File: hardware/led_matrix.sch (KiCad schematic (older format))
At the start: 16 parts

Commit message: Rev5 schematic changes and pcb cleanup
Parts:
- added R11, R26, R6: R, Resistor_SMD:R_0603_1608Metric, symbol Device:R
- added U10, U11, U9: SM16106, Package_SO:QSOP-24_3.9x8.7mm_P0.635mm, symbol rgbchip:SM16106
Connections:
- net L2 is gone; now on net VCC: D43.4 (A), D47.4 (A)
- net L3 is gone; now on net VCC: D36.4 (A), D40.4 (A)
- net L4 is gone; now on net VCC: D44.4 (A), D48.4 (A)
- net L5 is gone; now on net VCC: D37.4 (A), D41.4 (A)
- net L6 is gone; now on net VCC: D45.4 (A), D49.4 (A)
- net L7 is gone; now on net VCC: D38.4 (A), D42.4 (A)
- net L8 is gone; now on net VCC: D46.4 (A), D50.4 (A)
- net B1: now also U11.5 (OUT0); no longer D36.3 (BK), D37.3 (BK), D38.3 (BK), D43.3 (BK), D44.3 (BK), D45.3 (BK), D46.3 (BK)
- net B2: now also U11.6 (OUT1); no longer D40.3 (BK), D41.3 (BK), D42.3 (BK), D47.3 (BK), D48.3 (BK), D49.3 (BK), D50.3 (BK)
- net G1: now also U10.5 (OUT0); no longer D36.2 (GK), D37.2 (GK), D38.2 (GK), D43.2 (GK), D44.2 (GK), D45.2 (GK), D46.2 (GK)
- net G2: now also U10.6 (OUT1); no longer D40.2 (GK), D41.2 (GK), D42.2 (GK), D47.2 (GK), D48.2 (GK), D49.2 (GK), D50.2 (GK)
- net R1: now also U9.5 (OUT0); no longer D36.1 (RK), D37.1 (RK), D38.1 (RK), D43.1 (RK), D44.1 (RK), D45.1 (RK), D46.1 (RK)
- net R2: now also U9.6 (OUT1); no longer D40.1 (RK), D41.1 (RK), D42.1 (RK), D47.1 (RK), D48.1 (RK), D49.1 (RK), D50.1 (RK)
- net L1 renamed VCC
- net VCC: now also U10.24 (VDD), U11.24 (VDD), U9.24 (VDD)
- new net: U10.2 (SDI), U9.22 (SDO)
- new net: R6.1, U9.23 (R-EXT)
- new net: U10.22 (SDO), U11.2 (SDI)
- new net: R26.1, U11.23 (R-EXT)
- new net: R11.1, U10.23 (R-EXT)
- new net B10: D41.3 (BK), U11.14 (OUT9)
- new net B11: D45.3 (BK), U11.15 (OUT10)
- new net B12: D49.3 (BK), U11.16 (OUT11)
- new net B13: D38.3 (BK), U11.17 (OUT12)
- new net B14: D42.3 (BK), U11.18 (OUT13)
- new net B15: D46.3 (BK), U11.19 (OUT14)
- new net B16: D50.3 (BK), U11.20 (OUT15)
- new net B3: D43.3 (BK), U11.7 (OUT2)
- new net B4: D47.3 (BK), U11.8 (OUT3)
- new net B5: D36.3 (BK), U11.9 (OUT4)
- new net B6: D40.3 (BK), U11.10 (OUT5)
- new net B7: D44.3 (BK), U11.11 (OUT6)
- new net B8: D48.3 (BK), U11.12 (OUT7)
- new net B9: D37.3 (BK), U11.13 (OUT8)
- new net CLK: U10.3 (CLK), U11.3 (CLK), U9.3 (CLK)
- new net G10: D41.2 (GK), U10.14 (OUT9)
- new net G11: D45.2 (GK), U10.15 (OUT10)
- new net G12: D49.2 (GK), U10.16 (OUT11)
- new net G13: D38.2 (GK), U10.17 (OUT12)
- new net G14: D42.2 (GK), U10.18 (OUT13)
- new net G15: D46.2 (GK), U10.19 (OUT14)
- new net G16: D50.2 (GK), U10.20 (OUT15)
- new net G3: D43.2 (GK), U10.7 (OUT2)
- new net G4: D47.2 (GK), U10.8 (OUT3)
- new net G5: D36.2 (GK), U10.9 (OUT4)
- new net G6: D40.2 (GK), U10.10 (OUT5)
- new net G7: D44.2 (GK), U10.11 (OUT6)
- new net G8: D48.2 (GK), U10.12 (OUT7)
- new net G9: D37.2 (GK), U10.13 (OUT8)
- new net GND: R11.2, R26.2, R6.2, U10.1 (GND), U11.1 (GND), U9.1 (GND)
- new net LE: U10.4 (LE), U11.4 (LE), U9.4 (LE)
- new net OE: U10.21 (OE), U11.21 (OE), U9.21 (OE)
- new net R10: D41.1 (RK), U9.14 (OUT9)
- new net R11: D45.1 (RK), U9.15 (OUT10)
- new net R12: D49.1 (RK), U9.16 (OUT11)
- new net R13: D38.1 (RK), U9.17 (OUT12)
- new net R14: D42.1 (RK), U9.18 (OUT13)
- new net R15: D46.1 (RK), U9.19 (OUT14)
- new net R16: D50.1 (RK), U9.20 (OUT15)
- new net R3: D43.1 (RK), U9.7 (OUT2)
- new net R4: D47.1 (RK), U9.8 (OUT3)
- new net R5: D36.1 (RK), U9.9 (OUT4)
- new net R6: D40.1 (RK), U9.10 (OUT5)
- new net R7: D44.1 (RK), U9.11 (OUT6)
- new net R8: D48.1 (RK), U9.12 (OUT7)
- new net R9: D37.1 (RK), U9.13 (OUT8)
- new net SDI: U9.2 (SDI)
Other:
- moved on the sheet: D35, D36, D37, D38, D39, D40, D41, D42, D43, D44, D45, D46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

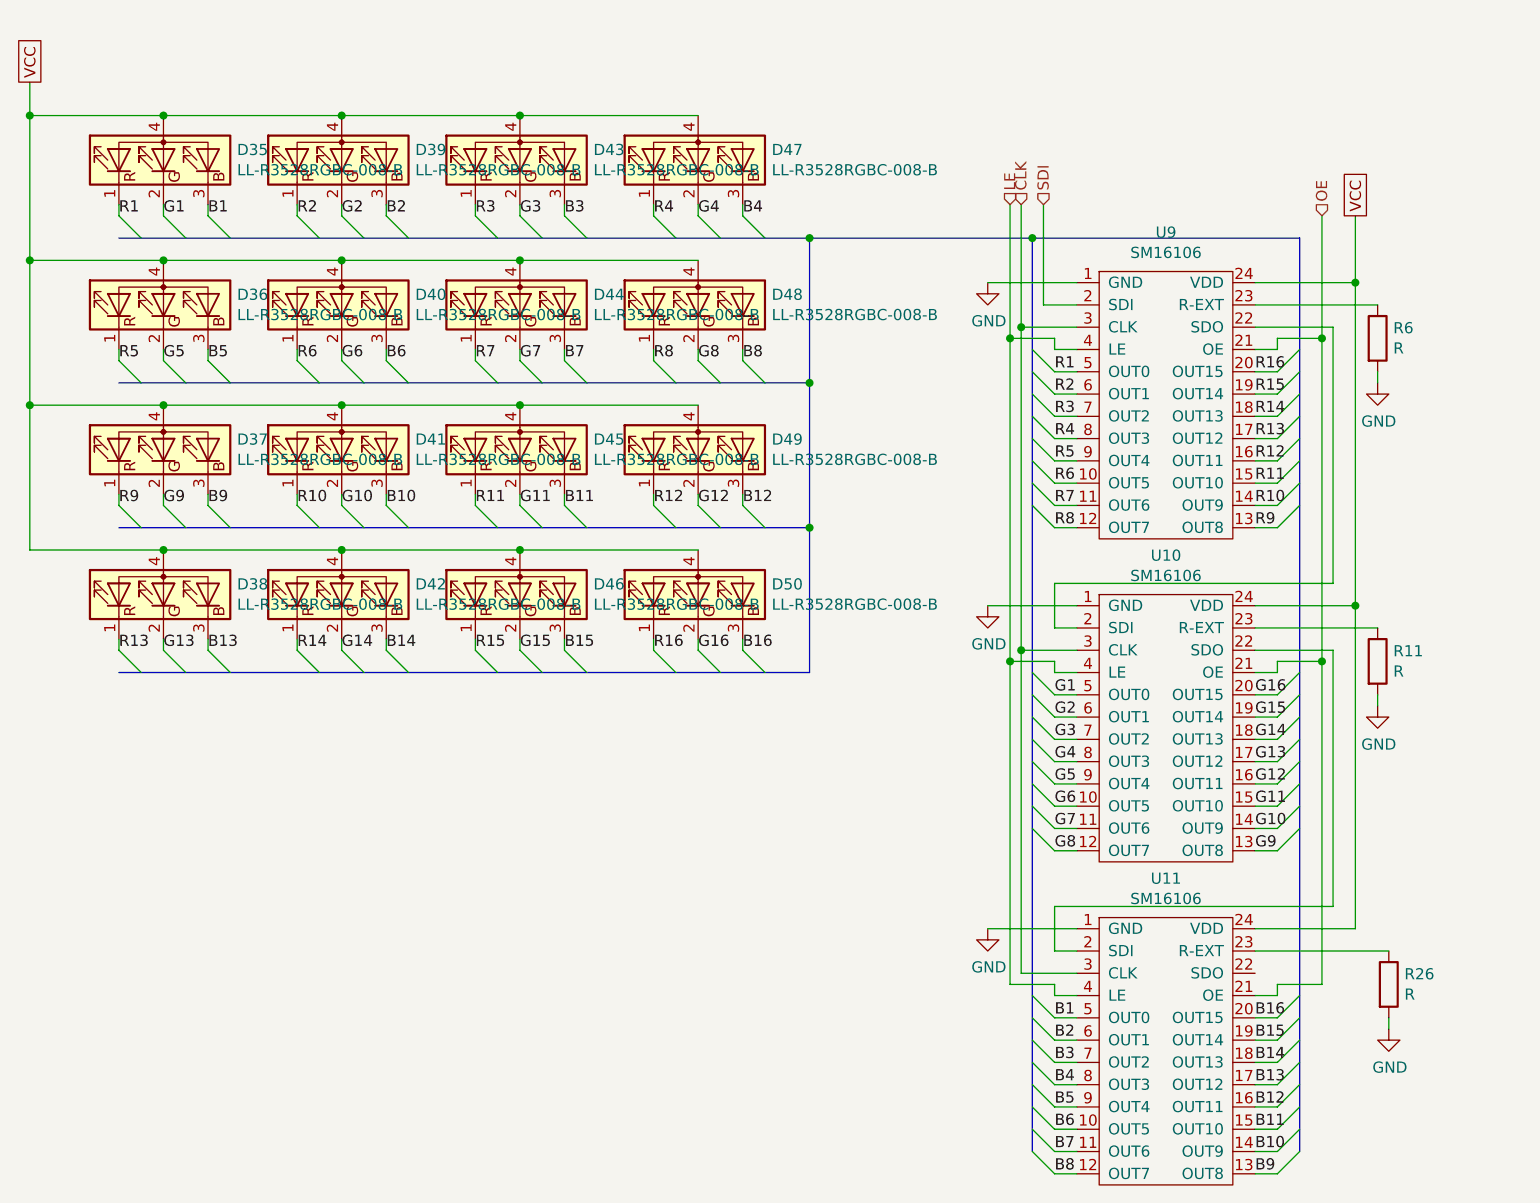
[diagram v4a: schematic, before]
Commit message: Major routing of the led matrix done
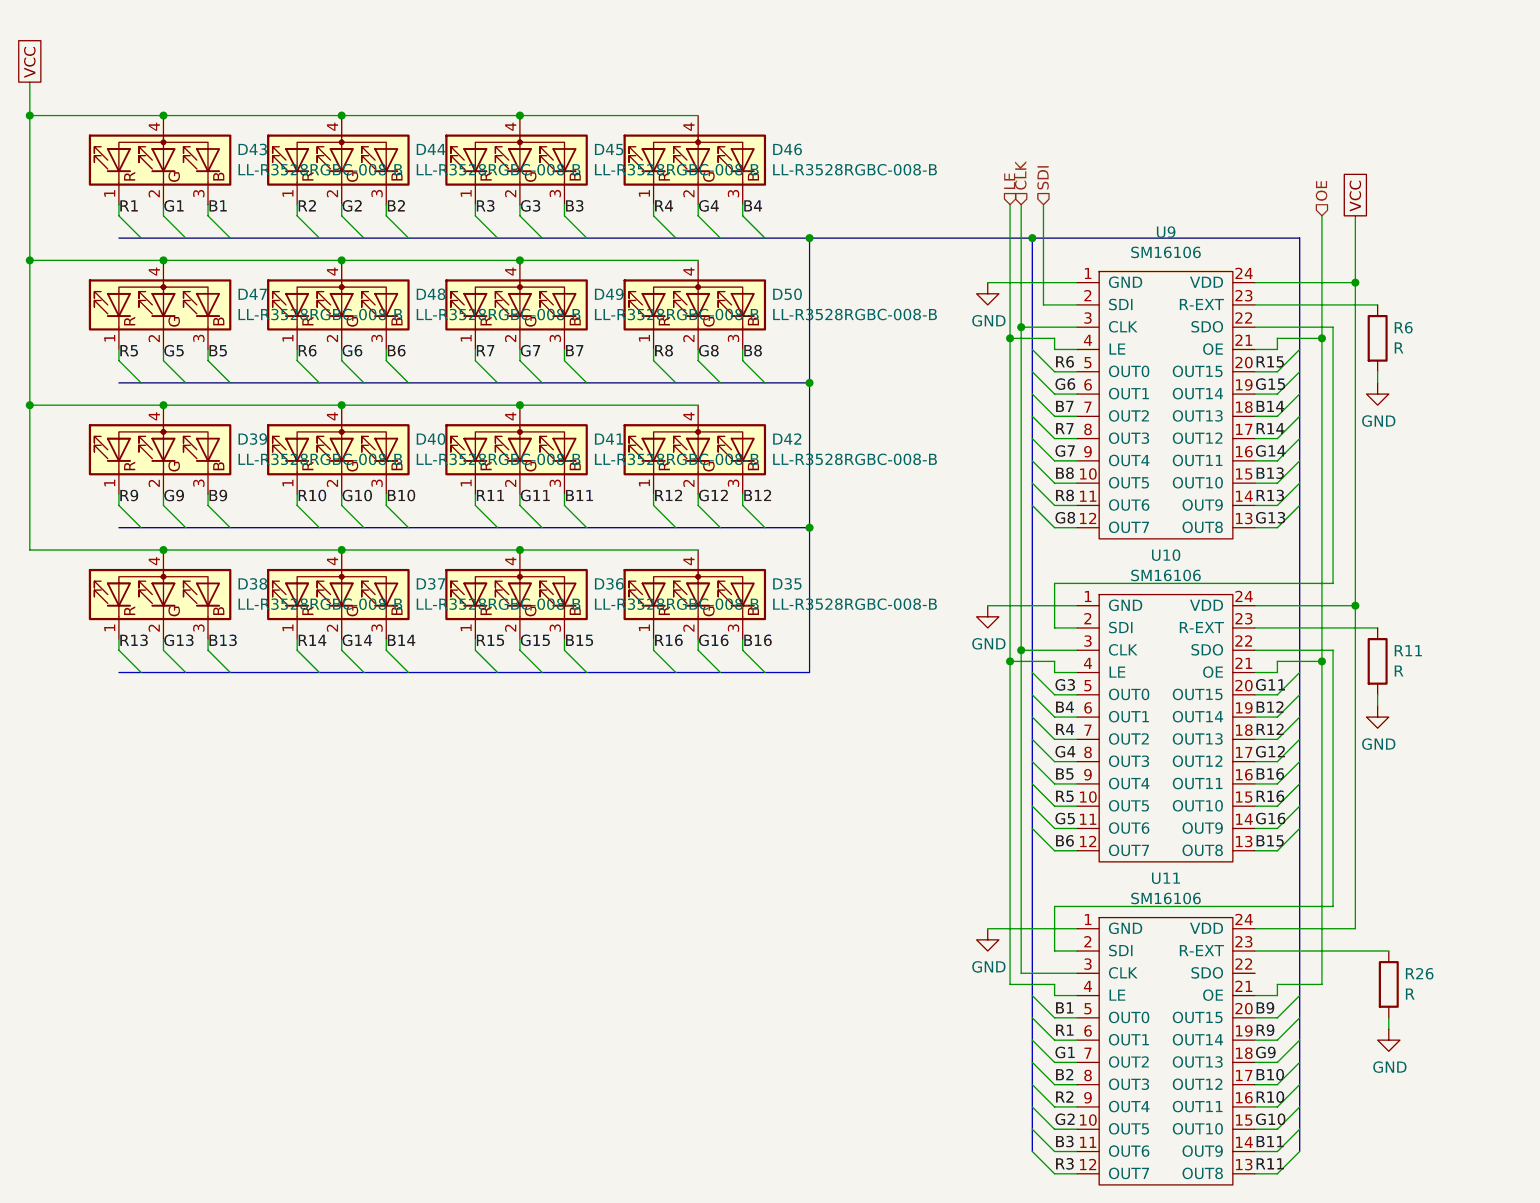
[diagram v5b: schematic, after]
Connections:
- net B1: now also D43.3 (BK); no longer D35.3 (BK)
- net B10: now also D40.3 (BK), U11.17 (OUT12); no longer D41.3 (BK), U11.14 (OUT9)
- net B11: now also D41.3 (BK), U11.14 (OUT9); no longer D45.3 (BK), U11.15 (OUT10)
- net B12: now also D42.3 (BK), U10.19 (OUT14); no longer D49.3 (BK), U11.16 (OUT11)
- net B13: now also U9.15 (OUT10); no longer U11.17 (OUT12)
- net B14: now also D37.3 (BK), U9.18 (OUT13); no longer D42.3 (BK), U11.18 (OUT13)
- net B15: now also D36.3 (BK), U10.13 (OUT8); no longer D46.3 (BK), U11.19 (OUT14)
- net B16: now also D35.3 (BK), U10.16 (OUT11); no longer D50.3 (BK), U11.20 (OUT15)
- net B2: now also D44.3 (BK), U11.8 (OUT3); no longer D39.3 (BK), U11.6 (OUT1)
- net B3: now also D45.3 (BK), U11.11 (OUT6); no longer D43.3 (BK), U11.7 (OUT2)
- net B4: now also D46.3 (BK), U10.6 (OUT1); no longer D47.3 (BK), U11.8 (OUT3)
- net B5: now also D47.3 (BK), U10.9 (OUT4); no longer D36.3 (BK), U11.9 (OUT4)
- net B6: now also D48.3 (BK), U10.12 (OUT7); no longer D40.3 (BK), U11.10 (OUT5)
- net B7: now also D49.3 (BK), U9.7 (OUT2); no longer D44.3 (BK), U11.11 (OUT6)
- net B8: now also D50.3 (BK), U9.10 (OUT5); no longer D48.3 (BK), U11.12 (OUT7)
- net B9: now also D39.3 (BK), U11.20 (OUT15); no longer D37.3 (BK), U11.13 (OUT8)
- net G1: now also D43.2 (GK), U11.7 (OUT2); no longer D35.2 (GK), U10.5 (OUT0)
- net G10: now also D40.2 (GK), U11.15 (OUT10); no longer D41.2 (GK), U10.14 (OUT9)
- net G11: now also D41.2 (GK), U10.20 (OUT15); no longer D45.2 (GK), U10.15 (OUT10)
- net G12: now also D42.2 (GK), U10.17 (OUT12); no longer D49.2 (GK), U10.16 (OUT11)
- net G13: now also U9.13 (OUT8); no longer U10.17 (OUT12)
- net G14: now also D37.2 (GK), U9.16 (OUT11); no longer D42.2 (GK), U10.18 (OUT13)
- net G15: now also D36.2 (GK), U9.19 (OUT14); no longer D46.2 (GK), U10.19 (OUT14)
- net G16: now also D35.2 (GK), U10.14 (OUT9); no longer D50.2 (GK), U10.20 (OUT15)
- net G2: now also D44.2 (GK), U11.10 (OUT5); no longer D39.2 (GK), U10.6 (OUT1)
- net G3: now also D45.2 (GK), U10.5 (OUT0); no longer D43.2 (GK), U10.7 (OUT2)
- net G4: now also D46.2 (GK); no longer D47.2 (GK)
- net G5: now also D47.2 (GK), U10.11 (OUT6); no longer D36.2 (GK), U10.9 (OUT4)
- net G6: now also D48.2 (GK), U9.6 (OUT1); no longer D40.2 (GK), U10.10 (OUT5)
- net G7: now also D49.2 (GK), U9.9 (OUT4); no longer D44.2 (GK), U10.11 (OUT6)
- net G8: now also D50.2 (GK), U9.12 (OUT7); no longer D48.2 (GK), U10.12 (OUT7)
- net G9: now also D39.2 (GK), U11.18 (OUT13); no longer D37.2 (GK), U10.13 (OUT8)
- net R1: now also D43.1 (RK), U11.6 (OUT1); no longer D35.1 (RK), U9.5 (OUT0)
- net R10: now also D40.1 (RK), U11.16 (OUT11); no longer D41.1 (RK), U9.14 (OUT9)
- net R11: now also D41.1 (RK), U11.13 (OUT8); no longer D45.1 (RK), U9.15 (OUT10)
- net R12: now also D42.1 (RK), U10.18 (OUT13); no longer D49.1 (RK), U9.16 (OUT11)
- net R13: now also U9.14 (OUT9); no longer U9.17 (OUT12)
- net R14: now also D37.1 (RK), U9.17 (OUT12); no longer D42.1 (RK), U9.18 (OUT13)
- net R15: now also D36.1 (RK), U9.20 (OUT15); no longer D46.1 (RK), U9.19 (OUT14)
- net R16: now also D35.1 (RK), U10.15 (OUT10); no longer D50.1 (RK), U9.20 (OUT15)
- net R2: now also D44.1 (RK), U11.9 (OUT4); no longer D39.1 (RK), U9.6 (OUT1)
- net R3: now also D45.1 (RK), U11.12 (OUT7); no longer D43.1 (RK), U9.7 (OUT2)
- net R4: now also D46.1 (RK), U10.7 (OUT2); no longer D47.1 (RK), U9.8 (OUT3)
- net R5: now also D47.1 (RK), U10.10 (OUT5); no longer D36.1 (RK), U9.9 (OUT4)
- net R6: now also D48.1 (RK), U9.5 (OUT0); no longer D40.1 (RK), U9.10 (OUT5)
- net R7: now also D49.1 (RK), U9.8 (OUT3); no longer D44.1 (RK), U9.11 (OUT6)
- net R8: now also D50.1 (RK), U9.11 (OUT6); no longer D48.1 (RK), U9.12 (OUT7)
- net R9: now also D39.1 (RK), U11.19 (OUT14); no longer D37.1 (RK), U9.13 (OUT8)
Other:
- moved on the sheet: D35, D36, D37, D39, D40, D41, D42, D43, D44, D45, D46, D47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

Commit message: Filled in rext value
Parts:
- R11, R26, R6: value R -> 820
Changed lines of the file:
@@
 P 8750 5150
 F 0 "R26" H 8820 5196 50  0000 L CNN
-F 1 "R" H 8820 5105 50  0000 L CNN
+F 1 "820" H 8820 5105 50  0000 L CNN
 F 2 "Resistor_SMD:R_0603_1608Metric" V 8680 5150 50  0001 C CNN
 F 3 "~" H 8750 5150 50  0001 C CNN
@@
 P 8700 3700
 F 0 "R11" H 8770 3746 50  0000 L CNN
-F 1 "R" H 8770 3655 50  0000 L CNN
+F 1 "820" H 8770 3655 50  0000 L CNN
 F 2 "Resistor_SMD:R_0603_1608Metric" V 8630 3700 50  0001 C CNN
 F 3 "~" H 8700 3700 50  0001 C CNN
@@
 P 8700 2250
 F 0 "R6" H 8770 2296 50  0000 L CNN
-F 1 "R" H 8770 2205 50  0000 L CNN
+F 1 "820" H 8770 2205 50  0000 L CNN
 F 2 "Resistor_SMD:R_0603_1608Metric" V 8630 2250 50  0001 C CNN
 F 3 "~" H 8700 2250 50  0001 C CNN
@@
 Wire Wire Line
 	8700 2100 8150 2100
-Wire Bus Line
-	3050 1800 6150 1800
-Wire Bus Line
-	3050 2450 6150 2450
-Wire Bus Line
-	3050 3100 6150 3100
-Wire Bus Line
-	3050 3750 6150 3750
-Wire Bus Line
-	7150 1800 7150 5900
-Wire Bus Line
-	8350 1800 8350 5900
 $Comp
 L Device:LED_RGBA D41
@@
 	0    -1   -1   0
 $EndComp
+Wire Bus Line
+	3050 1800 6150 1800
+Wire Bus Line
+	3050 2450 6150 2450
+Wire Bus Line
+	3050 3100 6150 3100
+Wire Bus Line
+	3050 3750 6150 3750
+Wire Bus Line
+	7150 1800 7150 5900
+Wire Bus Line
+	8350 1800 8350 5900
 $EndSCHEMATC

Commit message: Fixed BOM lines
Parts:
- R11, R26, R6: LCSC (none) -> C23253
- U10, U11, U9: LCSC (none) -> C121618
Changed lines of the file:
@@
 F 2 "Package_SO:QSOP-24_3.9x8.7mm_P0.635mm" H 7750 1900 50  0001 C CNN
 F 3 "" H 7750 1900 50  0001 C CNN
+F 4 "C121618" H 7750 1900 50  0001 C CNN "LCSC"
 	1    7750 1900
 	1    0    0    -1
@@
 F 2 "Package_SO:QSOP-24_3.9x8.7mm_P0.635mm" H 7750 3350 50  0001 C CNN
 F 3 "" H 7750 3350 50  0001 C CNN
+F 4 "C121618" H 7750 3350 50  0001 C CNN "LCSC"
 	1    7750 3350
 	1    0    0    -1
@@
 F 2 "Package_SO:QSOP-24_3.9x8.7mm_P0.635mm" H 7750 4800 50  0001 C CNN
 F 3 "" H 7750 4800 50  0001 C CNN
+F 4 "C121618" H 7750 4800 50  0001 C CNN "LCSC"
 	1    7750 4800
 	1    0    0    -1
@@
 F 2 "Resistor_SMD:R_0603_1608Metric" V 8680 5150 50  0001 C CNN
 F 3 "~" H 8750 5150 50  0001 C CNN
+F 4 "C23253" H 8750 5150 50  0001 C CNN "LCSC"
 	1    8750 5150
 	1    0    0    -1
@@
 F 2 "Resistor_SMD:R_0603_1608Metric" V 8630 3700 50  0001 C CNN
 F 3 "~" H 8700 3700 50  0001 C CNN
+F 4 "C23253" H 8700 3700 50  0001 C CNN "LCSC"
 	1    8700 3700
 	1    0    0    -1
@@
 F 2 "Resistor_SMD:R_0603_1608Metric" V 8630 2250 50  0001 C CNN
 F 3 "~" H 8700 2250 50  0001 C CNN
+F 4 "C23253" H 8700 2250 50  0001 C CNN "LCSC"
 	1    8700 2250
 	1    0    0    -1
